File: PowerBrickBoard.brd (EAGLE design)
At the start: 60.5 x 39.9 mm, 1 part

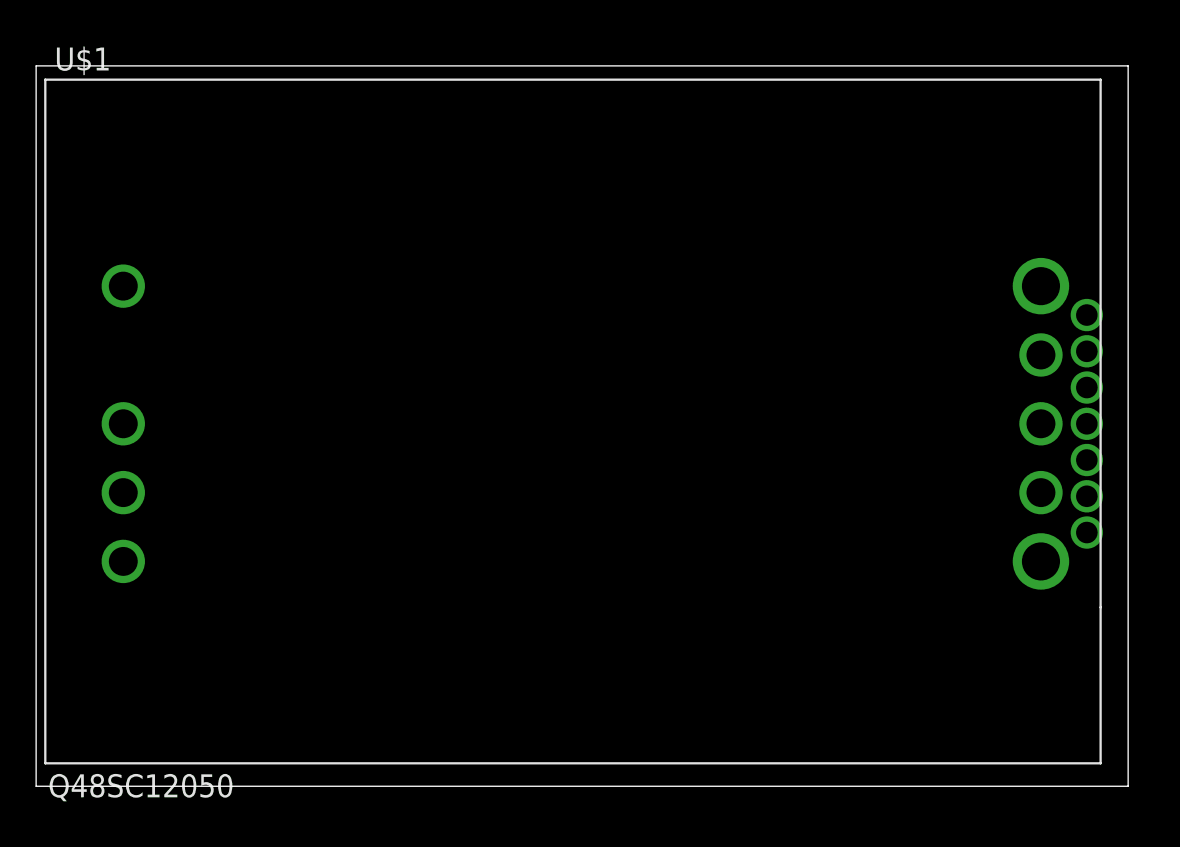
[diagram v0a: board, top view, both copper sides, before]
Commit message: added connectors
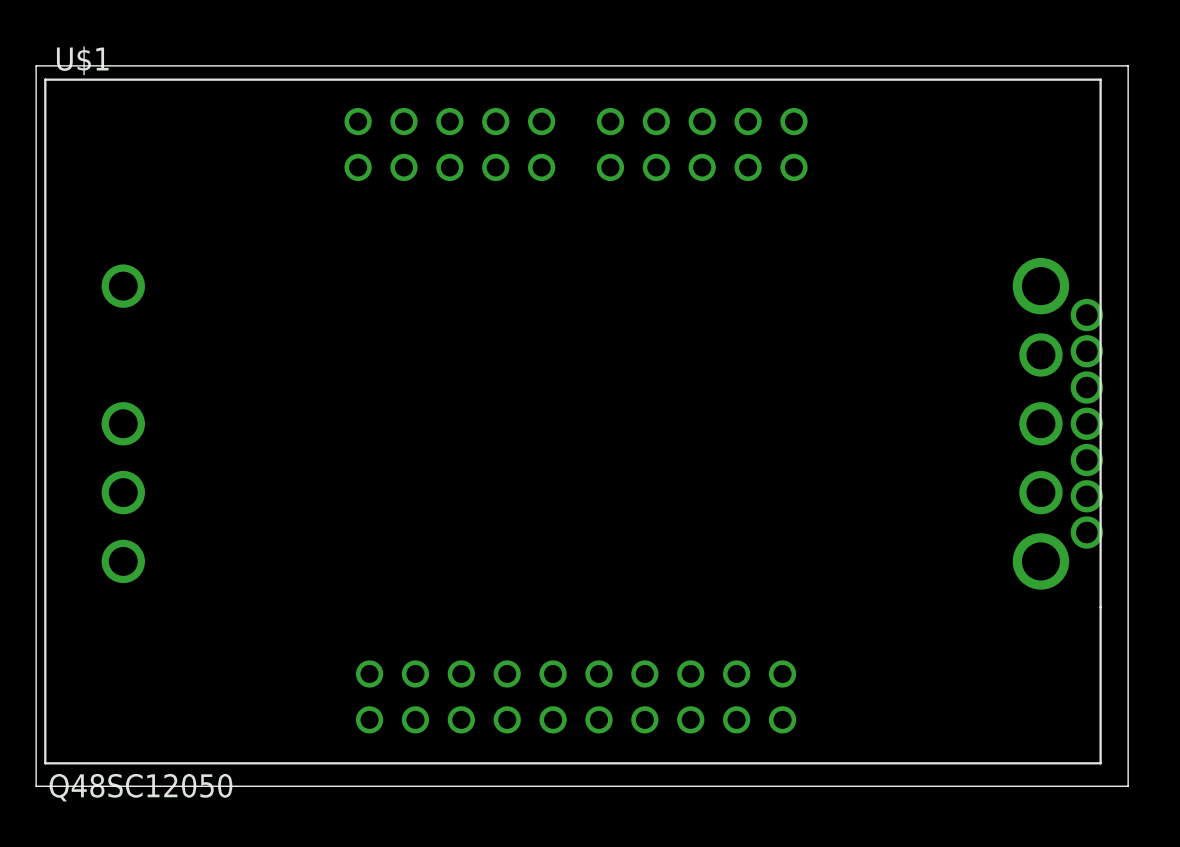
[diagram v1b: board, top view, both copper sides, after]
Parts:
- added U$2: BRICK_TO_POWER_DIST_WHOLE, PDB_TO_BRICKS:BRICK_TO_POWER_DIST_WHOLE
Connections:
- new net +12V: U$1.VOUT+, U$2.+12V1, U$2.+12V10, U$2.+12V2, U$2.+12V3, U$2.+12V4, U$2.+12V5, U$2.+12V6, U$2.+12V7, U$2.+12V8, U$2.+12V9
- new net +48V: U$1.VIN+, U$2.+48V1, U$2.+48V2, U$2.+48V3, U$2.+48V4
- new net 48V_GND: U$1.VIN-, U$2.48V_GND1, U$2.48V_GND2, U$2.48V_GND3, U$2.48V_GND4
- new net D_GND: U$1.DGND, U$2.D_GND
- new net GND: U$1.VOUT-, U$2.GND1, U$2.GND10, U$2.GND2, U$2.GND3, U$2.GND4, U$2.GND5, U$2.GND6, U$2.GND7, U$2.GND8, U$2.GND9
- new net ON/OFF: U$1.ON/OFF, U$2.ON/OFF

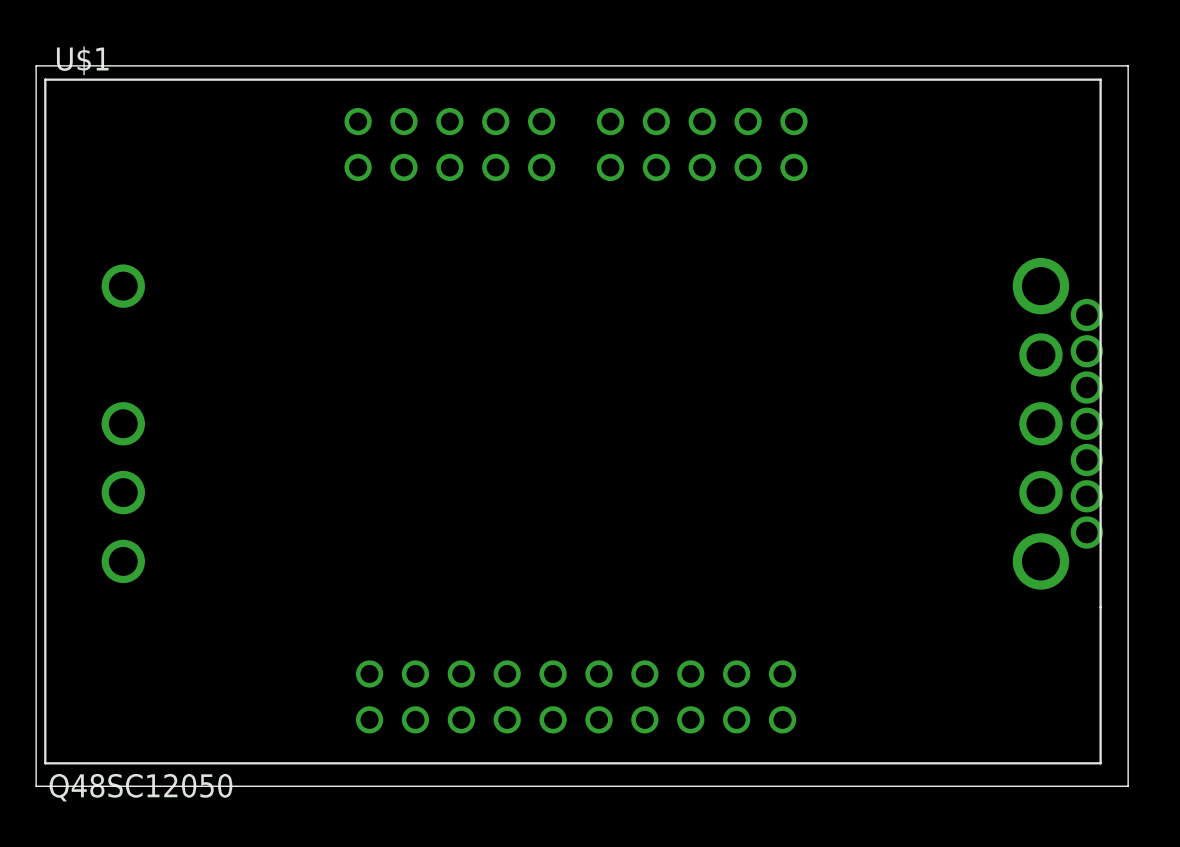
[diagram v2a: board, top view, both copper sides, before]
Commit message: Routed board
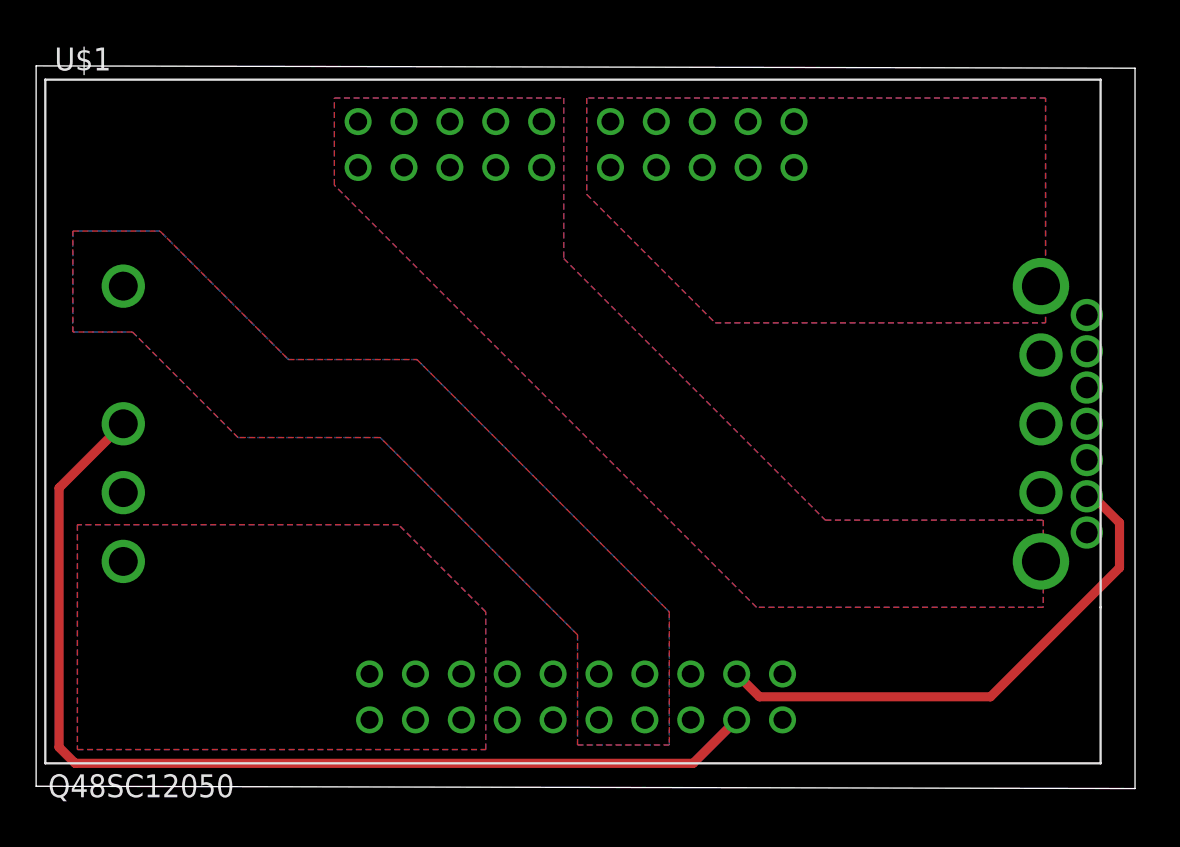
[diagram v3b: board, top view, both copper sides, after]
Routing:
- net ON/OFF: track 0.00 -> 58.3 mm
- net D_GND: track 0.00 -> 29.6 mm
- added copper zone on layer 1, net +12V
- added copper zone on layer 16, net +12V
- added copper zone on layer 1, net +48V
- added copper zone on layer 16, net +48V
- added copper zone on layer 1, net 48V_GND
- added copper zone on layer 16, net 48V_GND
- added copper zone on layer 1, net GND
- added copper zone on layer 16, net GND
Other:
- board size 60.5 x 39.9 mm -> 60.8 x 40 mm

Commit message: Updated d_gnd trace to be larger
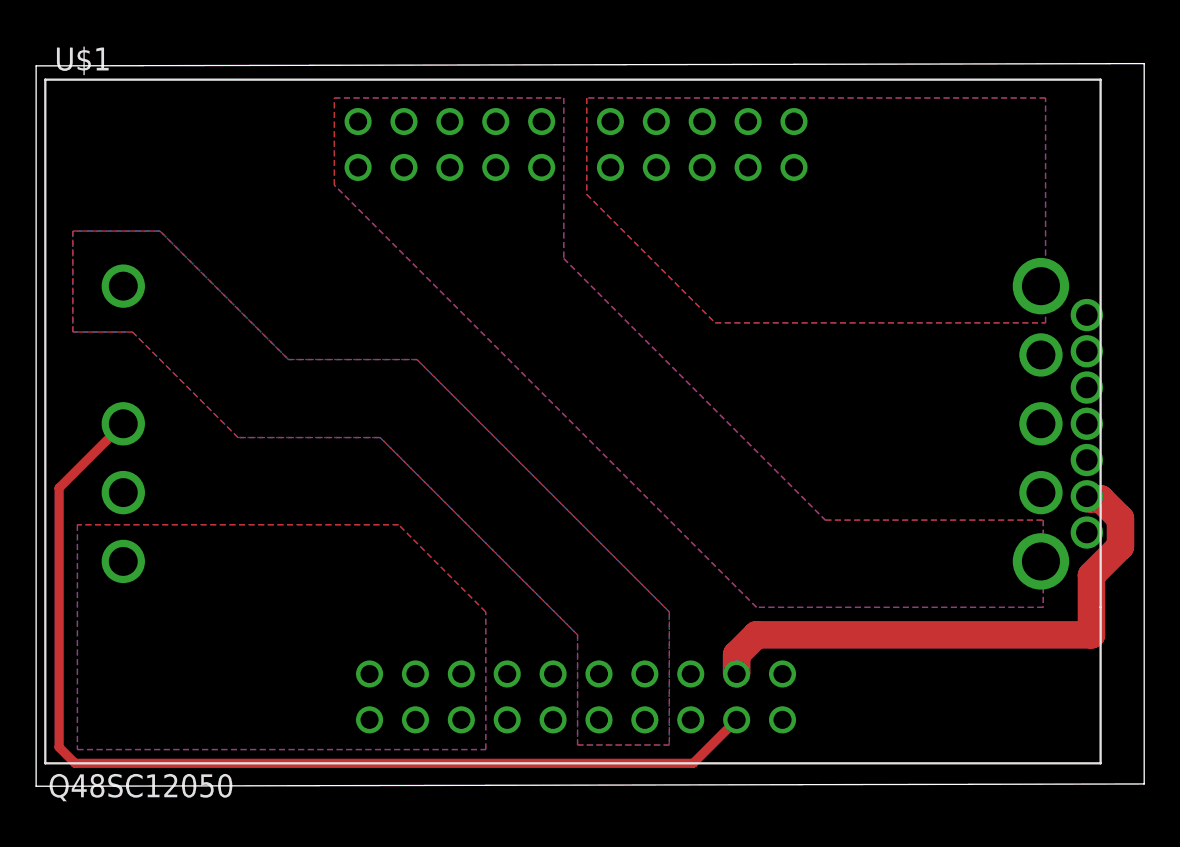
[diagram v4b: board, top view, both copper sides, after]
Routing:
- net D_GND: track 29.6 -> 30.6 mm
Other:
- board size 60.8 x 40 mm -> 61.3 x 40 mm
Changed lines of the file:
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@@
 <board>
 <plain>
-<wire x1="0.254" y1="0.254" x2="61.087" y2="0.127" width="0" layer="20"/>
-<wire x1="61.087" y1="0.127" x2="61.087" y2="40.005" width="0" layer="20"/>
-<wire x1="61.087" y1="40.005" x2="0.254" y2="40.132" width="0" layer="20"/>
+<wire x1="0.254" y1="0.254" x2="61.595" y2="0.381" width="0" layer="20"/>
+<wire x1="61.595" y1="0.381" x2="61.595" y2="40.259" width="0" layer="20"/>
+<wire x1="61.595" y1="40.259" x2="0.254" y2="40.132" width="0" layer="20"/>
 <wire x1="0.254" y1="40.132" x2="0.254" y2="0.254" width="0" layer="20"/>
 </plain>
@@
 <contactref element="U$1" pad="DGND"/>
 <contactref element="U$2" pad="D_GND"/>
-<wire x1="60.22975" y1="14.83940625" x2="58.76235625" y2="16.3068" width="0.508" layer="1"/>
-<wire x1="58.42" y1="16.3068" x2="58.76235625" y2="16.3068" width="0.508" layer="1"/>
-<wire x1="60.22975" y1="14.83940625" x2="60.22975" y2="12.35075" width="0.508" layer="1"/>
-<wire x1="40.296" y1="5.207" x2="39.033" y2="6.47" width="0.508" layer="1"/>
-<wire x1="60.22975" y1="12.35075" x2="53.086" y2="5.207" width="0.508" layer="1"/>
-<wire x1="53.086" y1="5.207" x2="40.296" y2="5.207" width="0.508" layer="1"/>
+<wire x1="39.033" y1="6.47" x2="39.033" y2="7.537" width="1.524" layer="1"/>
+<wire x1="39.033" y1="7.537" x2="40.132" y2="8.636" width="1.524" layer="1"/>
+<wire x1="40.132" y1="8.636" x2="58.674" y2="8.636" width="1.524" layer="1"/>
+<wire x1="60.28055" y1="13.52953125" x2="60.28055" y2="15.07086875" width="1.524" layer="1"/>
+<wire x1="60.28055" y1="15.07086875" x2="59.19066875" y2="16.16075" width="1.524" layer="1"/>
+<wire x1="59.19066875" y1="16.16075" x2="58.56605" y2="16.16075" width="1.524" layer="1"/>
+<wire x1="58.56605" y1="16.16075" x2="58.42" y2="16.3068" width="1.524" layer="1"/>
+<wire x1="58.674" y1="8.636" x2="58.674" y2="11.92298125" width="1.524" layer="1"/>
+<wire x1="58.674" y1="11.92298125" x2="60.28055" y2="13.52953125" width="1.524" layer="1"/>
 </signal>
 <signal name="+12V">
